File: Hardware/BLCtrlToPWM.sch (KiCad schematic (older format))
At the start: 30 parts, among them IC1 ATMEGA2560-A, Y1 16MHz

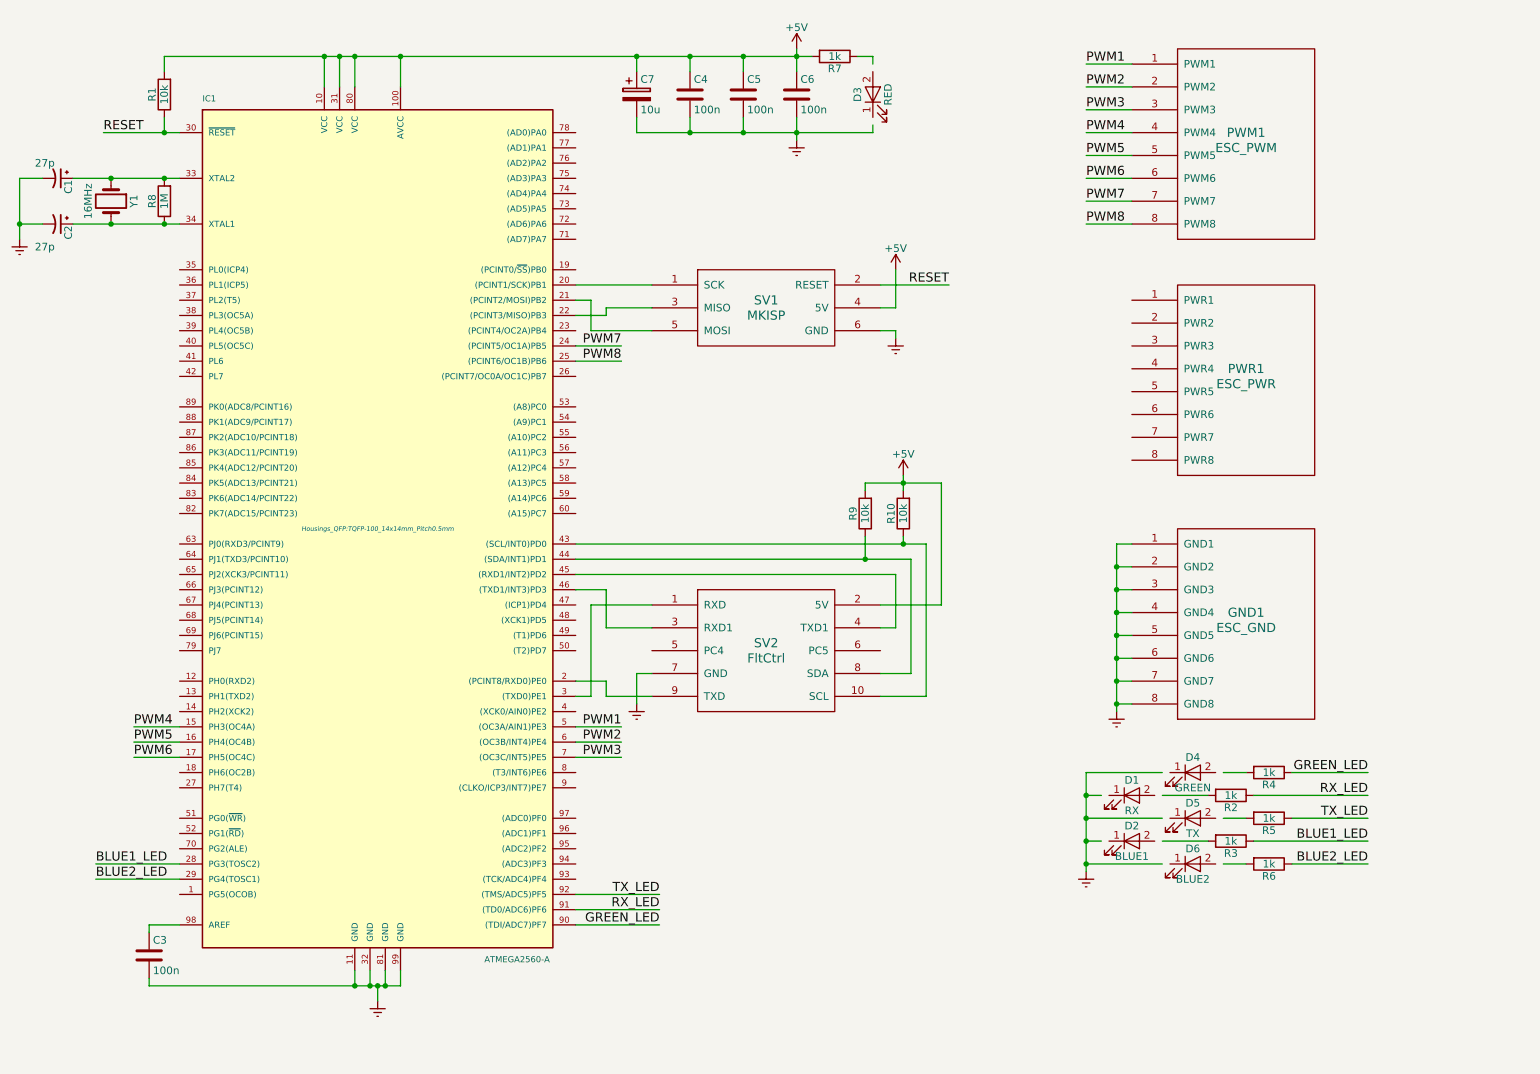
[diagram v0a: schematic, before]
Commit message: Added second debug serial output. Changed TX on existing serial linesto RX. Added N-MOSFETs to LEDs to remove current requrements on MCU. Added jumpers for power source selection (preferably use the BEC from the ESCs)
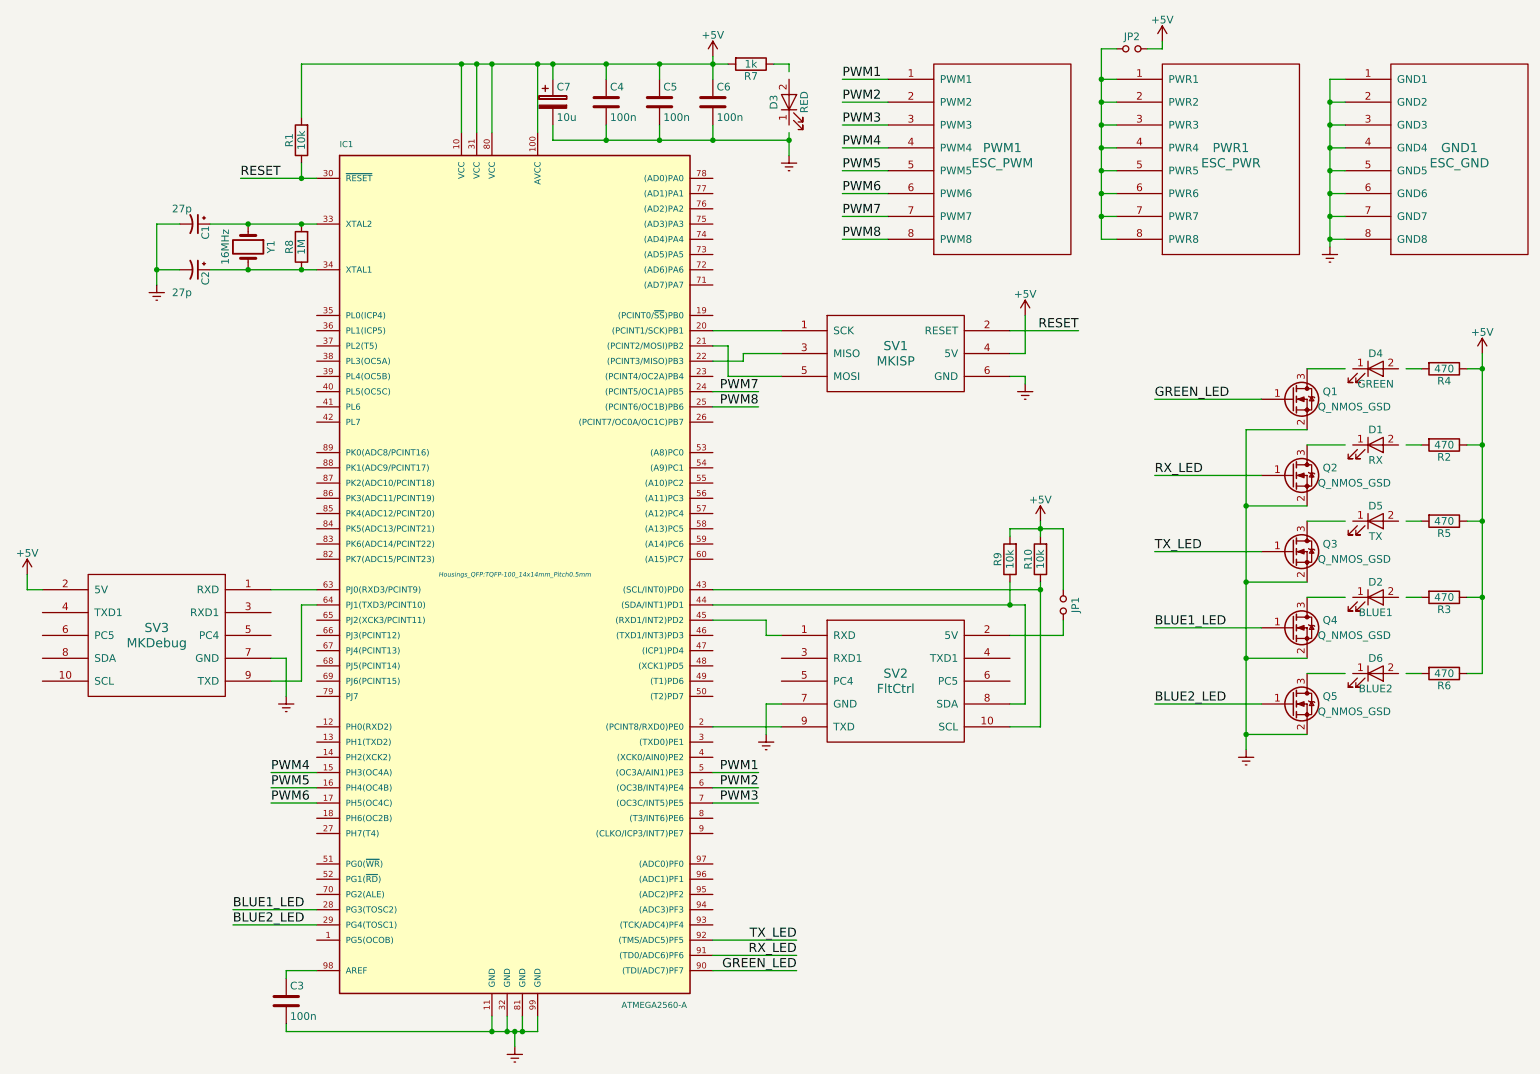
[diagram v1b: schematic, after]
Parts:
- added JP1, JP2: Jumper_NO_Small, Pin_Headers:Pin_Header_Straight_1x02, symbol Jumper_NO_Small
- added Q1, Q2, Q3, Q4, Q5: Q_NMOS_GSD, TO_SOT_Packages_SMD:SOT-23_Handsoldering, symbol Q_NMOS_GSD
- added SV3: MKDebug, Pin_Headers_Edge:Pin_Header_Edge_2x05, symbol FltCtrl
- R2, R3, R4, R5, R6: value 1k -> 470
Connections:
- wire segments 119 -> 142
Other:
- moved on the sheet: C1, C2, C3, C4, C5, C6, C7, D1, D2, D3, D4, D5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

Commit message: Finished board design for version 2
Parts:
- C1, C2: value 27p -> 22p
- Y1: footprint Crystals:Crystal_HC49-SD_SMD -> Crystals:Crystal_HC49-U_Vertical
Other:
- moved on the sheet: D1, D2, D4, D5, D6, R2, R3, R4, R5, R6
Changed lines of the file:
@@
 LIBS:mikrokopter
 LIBS:BLCtrlToPWM
+LIBS:BLCtrlToPWM-cache
 EELAYER 25 0
 EELAYER END
@@
 Sheet 1 1
 Title "BLCtrl Command to PWM Converter"
-Date "2016-12-15"
+Date "2017-01-04"
 Rev "2"
 Comp "University of Tokyo"
@@
 F 0 "Y1" H 2300 2350 50  0000 C CNN
 F 1 "16MHz" H 2300 2050 50  0000 C CNN
-F 2 "Crystals:Crystal_HC49-SD_SMD" H 2300 2200 60  0001 C CNN
+F 2 "Crystals:Crystal_HC49-U_Vertical" H 2300 2200 60  0001 C CNN
 F 3 "" H 2300 2200 60  0000 C CNN
 	1    2300 2200
@@
 P 1950 2050
 F 0 "C1" H 1960 2120 50  0000 L CNN
-F 1 "27p" V 1850 1900 50  0000 L CNN
+F 1 "22p" V 1850 1900 50  0000 L CNN
 F 2 "Capacitors_SMD:C_0805_HandSoldering" H 1950 2050 60  0001 C CNN
 F 3 "" H 1950 2050 60  0000 C CNN
@@
 P 1950 2350
 F 0 "C2" H 1960 2420 50  0000 L CNN
-F 1 "27p" V 2100 2200 50  0000 L CNN
+F 1 "22p" V 2100 2200 50  0000 L CNN
 F 2 "Capacitors_SMD:C_0805_HandSoldering" H 1950 2350 60  0001 C CNN
 F 3 "" H 1950 2350 60  0000 C CNN
@@
 L LED D1
 U 1 1 56360A2B
-P 9700 3500
-F 0 "D1" H 9700 3600 50  0000 C CNN
-F 1 "RX" H 9700 3400 50  0000 C CNN
-F 2 "LEDs:LED-0805" H 9700 3500 60  0001 C CNN
-F 3 "" H 9700 3500 60  0000 C CNN
-	1    9700 3500
+P 10100 3500
+F 0 "D1" H 10100 3600 50  0000 C CNN
+F 1 "RX" H 10100 3400 50  0000 C CNN
+F 2 "LEDs:LED-0805" H 10100 3500 60  0001 C CNN
+F 3 "" H 10100 3500 60  0000 C CNN
+	1    10100 3500
 	1    0    0    -1
 $EndComp
@@
 L LED D4
 U 1 1 56360A6F
-P 9700 3000
-F 0 "D4" H 9700 3100 50  0000 C CNN
-F 1 "GREEN" H 9700 2900 50  0000 C CNN
-F 2 "LEDs:LED-0805" H 9700 3000 60  0001 C CNN
-F 3 "" H 9700 3000 60  0000 C CNN
-	1    9700 3000
+P 10100 3000
+F 0 "D4" H 10100 3100 50  0000 C CNN
+F 1 "GREEN" H 10100 2900 50  0000 C CNN
+F 2 "LEDs:LED-0805" H 10100 3000 60  0001 C CNN
+F 3 "" H 10100 3000 60  0000 C CNN
+	1    10100 3000
 	1    0    0    -1
 $EndComp
@@
 L LED D5
 U 1 1 56360AB0
-P 9700 4000
-F 0 "D5" H 9700 4100 50  0000 C CNN
-F 1 "TX" H 9700 3900 50  0000 C CNN
-F 2 "LEDs:LED-0805" H 9700 4000 60  0001 C CNN
-F 3 "" H 9700 4000 60  0000 C CNN
-	1    9700 4000
+P 10100 4000
+F 0 "D5" H 10100 4100 50  0000 C CNN
+F 1 "TX" H 10100 3900 50  0000 C CNN
+F 2 "LEDs:LED-0805" H 10100 4000 60  0001 C CNN
+F 3 "" H 10100 4000 60  0000 C CNN
+	1    10100 4000
 	1    0    0    -1
 $EndComp
@@
 L R R2
 U 1 1 5636885F
-P 10150 3500
-F 0 "R2" V 10230 3500 50  0000 C CNN
-F 1 "470" V 10150 3500 50  0000 C CNN
-F 2 "Resistors_SMD:R_0805_HandSoldering" V 10080 3500 30  0001 C CNN
-F 3 "" H 10150 3500 30  0000 C CNN
-	1    10150 3500
+P 9650 3500
+F 0 "R2" V 9730 3500 50  0000 C CNN
+F 1 "470" V 9650 3500 50  0000 C CNN
+F 2 "Resistors_SMD:R_0805_HandSoldering" V 9580 3500 30  0001 C CNN
+F 3 "" H 9650 3500 30  0000 C CNN
+	1    9650 3500
 	0    1    1    0
 $EndComp
@@
 L R R4
 U 1 1 56368EC8
-P 10150 3000
-F 0 "R4" V 10230 3000 50  0000 C CNN
-F 1 "470" V 10150 3000 50  0000 C CNN
-F 2 "Resistors_SMD:R_0805_HandSoldering" V 10080 3000 30  0001 C CNN
-F 3 "" H 10150 3000 30  0000 C CNN
-	1    10150 3000
+P 9650 3000
+F 0 "R4" V 9730 3000 50  0000 C CNN
+F 1 "470" V 9650 3000 50  0000 C CNN
+F 2 "Resistors_SMD:R_0805_HandSoldering" V 9580 3000 30  0001 C CNN
+F 3 "" H 9650 3000 30  0000 C CNN
+	1    9650 3000
 	0    1    1    0
 $EndComp
@@
 L R R5
 U 1 1 56368F3C
-P 10150 4000
-F 0 "R5" V 10230 4000 50  0000 C CNN
-F 1 "470" V 10150 4000 50  0000 C CNN
-F 2 "Resistors_SMD:R_0805_HandSoldering" V 10080 4000 30  0001 C CNN
-F 3 "" H 10150 4000 30  0000 C CNN
-	1    10150 4000
+P 9650 4000
+F 0 "R5" V 9730 4000 50  0000 C CNN
+F 1 "470" V 9650 4000 50  0000 C CNN
+F 2 "Resistors_SMD:R_0805_HandSoldering" V 9580 4000 30  0001 C CNN
+F 3 "" H 9650 4000 30  0000 C CNN
+	1    9650 4000
 	0    1    1    0
 $EndComp
@@
 L R R3
 U 1 1 56368F99
-P 10150 4500
-F 0 "R3" V 10230 4500 50  0000 C CNN
-F 1 "470" V 10150 4500 50  0000 C CNN
-F 2 "Resistors_SMD:R_0805_HandSoldering" V 10080 4500 30  0001 C CNN
-F 3 "" H 10150 4500 30  0000 C CNN
-	1    10150 4500
+P 9650 4500
+F 0 "R3" V 9730 4500 50  0000 C CNN
+F 1 "470" V 9650 4500 50  0000 C CNN
+F 2 "Resistors_SMD:R_0805_HandSoldering" V 9580 4500 30  0001 C CNN
+F 3 "" H 9650 4500 30  0000 C CNN
+	1    9650 4500
 	0    1    1    0
 $EndComp
@@
 L R R6
 U 1 1 5636927D
-P 10150 5000
-F 0 "R6" V 10230 5000 50  0000 C CNN
-F 1 "470" V 10150 5000 50  0000 C CNN
-F 2 "Resistors_SMD:R_0805_HandSoldering" V 10080 5000 30  0001 C CNN
-F 3 "" H 10150 5000 30  0000 C CNN
-	1    10150 5000
+P 9650 5000
+F 0 "R6" V 9730 5000 50  0000 C CNN
+F 1 "470" V 9650 5000 50  0000 C CNN
+F 2 "Resistors_SMD:R_0805_HandSoldering" V 9580 5000 30  0001 C CNN
+F 3 "" H 9650 5000 30  0000 C CNN
+	1    9650 5000
 	0    1    1    0
 $EndComp
@@
 L LED D2
 U 1 1 56369996
-P 9700 4500
-F 0 "D2" H 9700 4600 50  0000 C CNN
-F 1 "BLUE1" H 9700 4400 50  0000 C CNN
-F 2 "LEDs:LED-0805" H 9700 4500 60  0001 C CNN
-F 3 "" H 9700 4500 60  0000 C CNN
-	1    9700 4500
+P 10100 4500
+F 0 "D2" H 10100 4600 50  0000 C CNN
+F 1 "BLUE1" H 10100 4400 50  0000 C CNN
+F 2 "LEDs:LED-0805" H 10100 4500 60  0001 C CNN
+F 3 "" H 10100 4500 60  0000 C CNN
+	1    10100 4500
 	1    0    0    -1
 $EndComp
@@
 L LED D6
 U 1 1 563699FA
-P 9700 5000
-F 0 "D6" H 9700 5100 50  0000 C CNN
-F 1 "BLUE2" H 9700 4900 50  0000 C CNN
-F 2 "LEDs:LED-0805" H 9700 5000 60  0001 C CNN
-F 3 "" H 9700 5000 60  0000 C CNN
-	1    9700 5000
+P 10100 5000
+F 0 "D6" H 10100 5100 50  0000 C CNN
+F 1 "BLUE2" H 10100 4900 50  0000 C CNN
+F 2 "LEDs:LED-0805" H 10100 5000 60  0001 C CNN
+F 3 "" H 10100 5000 60  0000 C CNN
+	1    10100 5000
 	1    0    0    -1
 $EndComp
@@
 	850  4450 850  4350
 Wire Wire Line
-	10000 3500 9900 3500
-Wire Wire Line
-	9900 3000 10000 3000
+	9900 3500 9800 3500
+Wire Wire Line
+	9800 3000 9900 3000
 Wire Wire Line
 	10400 2900 10400 5000
@@
 Connection ~ 10400 3000
 Wire Wire Line
-	10000 4000 9900 4000
-Wire Wire Line
-	10000 4500 9900 4500
-Wire Wire Line
-	10000 5000 9900 5000
+	9900 4000 9800 4000
+Wire Wire Line
+	9900 4500 9800 4500
+Wire Wire Line
+	9900 5000 9800 5000
 Wire Wire Line
 	9500 3000 9250 3000
